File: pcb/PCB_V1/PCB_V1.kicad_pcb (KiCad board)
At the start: 4 copper layers, 100 x 100 mm, 170 parts, among them J201 UART / 3V3 logic, J301 SHT4x / XH 2.50, J302 FLOAT / 3.5 mm, J401 HRO TF-01A, J501 FAN1 / 3.5 mm, J511 FAN2 / 3.5 mm, J521 PUMP 24V / 6W, J601 PTC + / switched - (3.5 mm), J711 LED +/- (return isolated), J721 LED +/- (return isolated), J731 LED +/- (return isolated), J901 XT60PW-M 24V IN, Q501 AO3400A, Q511 AO3400A, Q521 AO3422, Q601 NTMFS5C628NLT1G, Q711 AOD66923, Q721 AOD66923, SW201 RESET, SW202 BOOT, U101 TPS54202DDCR, U201 ESP32-WROOM-32E-N4, U301 PCF8563T/5, U601 UCC27524ADR, U700 SN74LVC1G08DBVR, U710 AL8853S-13, U720 AL8853S-13, U902 LMR16020PDDAR, Y301 32.768k 12.5pF

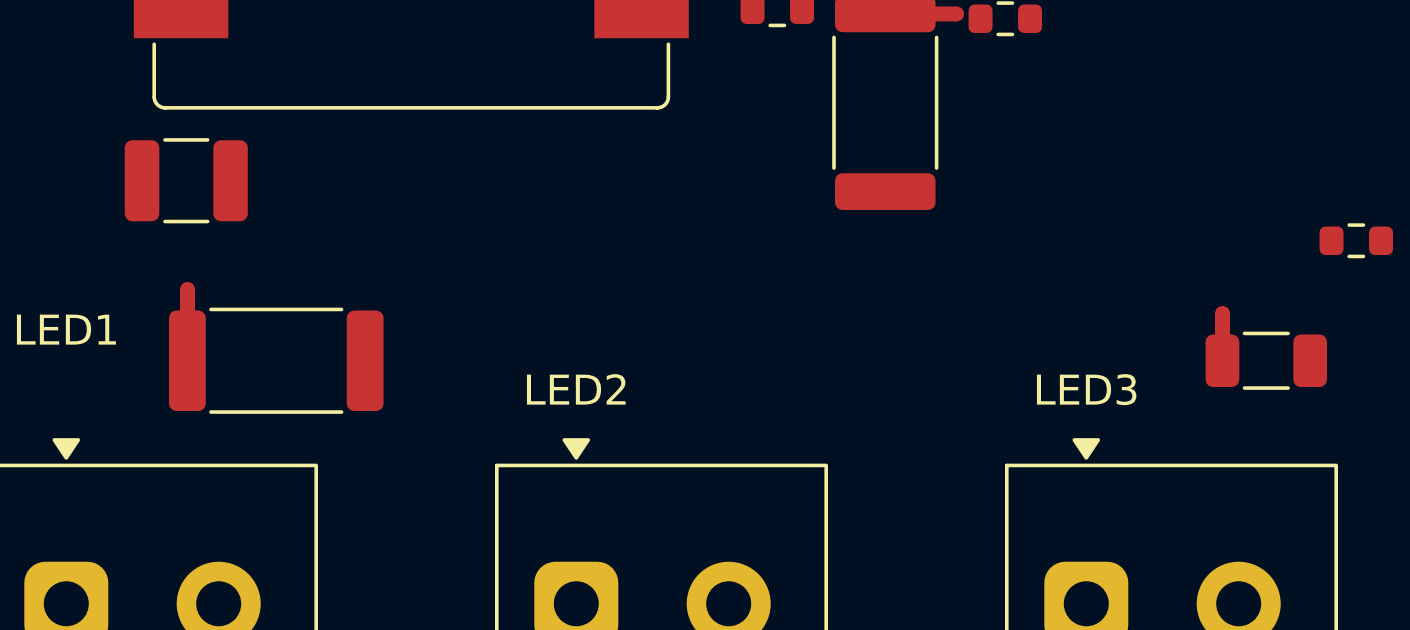
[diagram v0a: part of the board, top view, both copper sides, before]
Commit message: pcb: attach all 3D models to the board and check them
- sync_models.py --write attached the mechanical models (J901, J302,
  J501, J511, J521, J601, J711, J721, J731, F902, BT301, SW201, SW202);
  every placed part now has a 3D model.
- verify_placement.py fails when a placed part has no model or a
  ${KIPRJMOD} model file is missing.
- NT712/NT722 moved 0.1 mm away from R716/R726: 0.55 mm to the LED
  return pads, above the 0.5 mm LED48 clearance (the intermittent
  0.45 mm DRC report seen during PR #18).
- Checked in the KiCad 10 GUI 3D viewer (top, bottom with BT301,
  isometric) and the footprint editor 3D view; kicad-cli renders.
- F902 height stays calculated (17.15 mm); allow >= 18 mm until a
  sample is measured. SOURCES_mechanical.md and PLACEMENT.md updated.

Co-Authored-By: Claude Opus 5.5 <noreply@anthropic.com>
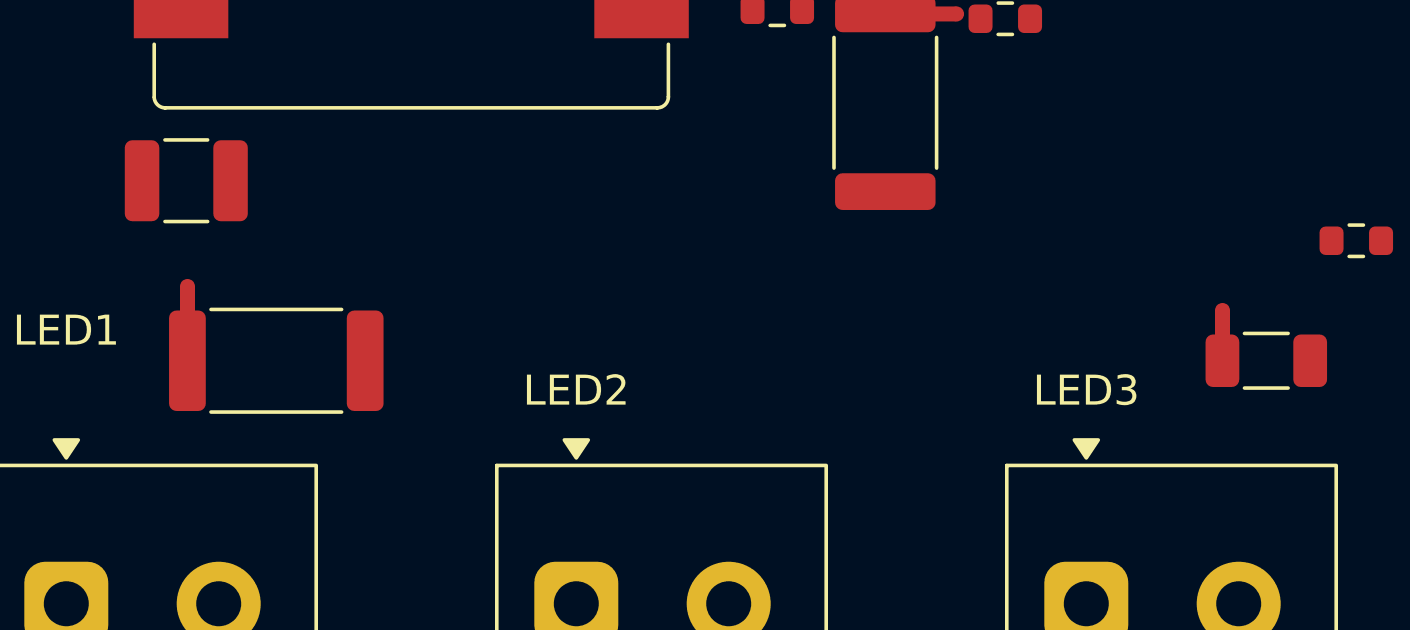
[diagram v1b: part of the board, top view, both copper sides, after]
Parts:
- moved NT722 0.10 mm to (98.5, 134.8)
- moved NT712 0.10 mm to (64.0, 134.0)
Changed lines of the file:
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@@
 		)
 		(embedded_fonts no)
+		(model "${KIPRJMOD}/libraries/GrowBox.3dshapes/TerminalBlock_DORABO_DB125-3.5_1x04_P3.50mm_Horizontal.step"
+			(offset
+				(xyz 0 0 0)
+			)
+			(scale
+				(xyz 1 1 1)
+			)
+			(rotate
+				(xyz 0 0 0)
+			)
+		)
 	)
 	(footprint "Capacitor_SMD:C_1210_3225Metric"
@@
 		)
 		(embedded_fonts no)
+		(model "${KIPRJMOD}/libraries/GrowBox.3dshapes/TerminalBlock_DORABO_DB125-3.5_1x04_P3.50mm_Horizontal.step"
+			(offset
+				(xyz 0 0 0)
+			)
+			(scale
+				(xyz 1 1 1)
+			)
+			(rotate
+				(xyz 0 0 0)
+			)
+		)
 	)
 	(footprint "Capacitor_SMD:C_0603_1608Metric"
@@
 		)
 		(embedded_fonts no)
+		(model "${KIPRJMOD}/libraries/GrowBox.3dshapes/TerminalBlock_DORABO_DB125-3.5_1x02_P3.50mm_Horizontal.step"
+			(offset
+				(xyz 0 0 0)
+			)
+			(scale
+				(xyz 1 1 1)
+			)
+			(rotate
+				(xyz 0 0 0)
+			)
+		)
 	)
 	(footprint "Button_Switch_SMD:SW_Push_1P1T_XKB_TS-1187A"
@@
 		)
 		(embedded_fonts no)
-		(model "${KICAD10_3DMODEL_DIR}/Button_Switch_SMD.3dshapes/SW_Push_1P1T_XKB_TS-1187A.step"
+		(model "${KIPRJMOD}/libraries/GrowBox.3dshapes/SW_Push_1P1T_XKB_TS-1187A.step"
 			(offset
 				(xyz 0 0 0)
@@
 		)
 		(embedded_fonts no)
+		(model "${KIPRJMOD}/libraries/GrowBox.3dshapes/TerminalBlock_DORABO_DB125-3.5_1x02_P3.50mm_Horizontal.step"
+			(offset
+				(xyz 0 0 0)
+			)
+			(scale
+				(xyz 1 1 1)
+			)
+			(rotate
+				(xyz 0 0 0)
+			)
+		)
 	)
 	(footprint "Capacitor_SMD:C_1210_3225Metric"
@@
 		)
 		(embedded_fonts no)
-		(model "${KICAD10_3DMODEL_DIR}/Connector_AMASS.3dshapes/AMASS_XT60PW-M_1x02_P7.20mm_Horizontal.step"
+		(model "${KIPRJMOD}/libraries/GrowBox.3dshapes/AMASS_XT60PW-M_1x02_P7.20mm_Horizontal.step"
 			(offset
 				(xyz 0 0 0)
@@
 		)
 		(embedded_fonts no)
+		(model "${KIPRJMOD}/libraries/GrowBox.3dshapes/TerminalBlock_KANGNEX_WJ500V-5.08_1x02_P5.08mm_Horizontal.step"
+			(offset
+				(xyz 0 0 0)
+			)
+			(scale
+				(xyz 1 1 1)
+			)
+			(rotate
+				(xyz 0 0 0)
+			)
+		)
 	)
 	(footprint "TestPoint:TestPoint_Pad_D2.0mm"
@@
 		)
 		(embedded_fonts no)
+		(model "${KIPRJMOD}/libraries/GrowBox.3dshapes/TerminalBlock_DORABO_DB125-3.5_1x02_P3.50mm_Horizontal.step"
+			(offset
+				(xyz 0 0 0)
+			)
+			(scale
+				(xyz 1 1 1)
+			)
+			(rotate
+				(xyz 0 0 0)
+			)
+		)
 	)
 	(footprint "Button_Switch_SMD:SW_Push_1P1T_XKB_TS-1187A"
@@
 		)
 		(embedded_fonts no)
-		(model "${KICAD10_3DMODEL_DIR}/Button_Switch_SMD.3dshapes/SW_Push_1P1T_XKB_TS-1187A.step"
+		(model "${KIPRJMOD}/libraries/GrowBox.3dshapes/SW_Push_1P1T_XKB_TS-1187A.step"
 			(offset
 				(xyz 0 0 0)
@@
 	(footprint "NetTie:NetTie-2_SMD_Pad0.5mm"
 		(layer "F.Cu")
-		(at 64.04 134.125 90)
+		(at 64.04 134.025 90)
 		(descr "Net tie, 2 pin, 0.5mm square SMD pads")
 		(tags "net tie")
@@
 		)
 		(embedded_fonts no)
+		(model "${KIPRJMOD}/libraries/GrowBox.3dshapes/TerminalBlock_KANGNEX_WJ500V-5.08_1x02_P5.08mm_Horizontal.step"
+			(offset
+				(xyz 0 0 0)
+			)
+			(scale
+				(xyz 1 1 1)
+			)
+			(rotate
+				(xyz 0 0 0)
+			)
+		)
 	)
 	(footprint "Capacitor_SMD:C_0603_1608Metric"
@@
 		)
 		(embedded_fonts no)
+		(model "${KIPRJMOD}/libraries/GrowBox.3dshapes/TerminalBlock_KANGNEX_WJ500V-5.08_1x02_P5.08mm_Horizontal.step"
+			(offset
+				(xyz 0 0 0)
+			)
+			(scale
+				(xyz 1 1 1)
+			)
+			(rotate
+				(xyz 0 0 0)
+			)
+		)
 	)
 	(footprint "Resistor_SMD:R_0603_1608Metric"
@@
 		)
 		(embedded_fonts no)
+		(model "${KIPRJMOD}/libraries/GrowBox.3dshapes/Fuseholder_Blade_Mini_XFCN_XF-508P.step"
+			(offset
+				(xyz 0 0 0)
+			)
+			(scale
+				(xyz 1 1 1)
+			)
+			(rotate
+				(xyz 0 0 0)
+			)
+		)
 	)
 	(footprint "NetTie:NetTie-2_SMD_Pad0.5mm"
 		(layer "F.Cu")
-		(at 98.54 134.925 90)
+		(at 98.54 134.825 90)
 		(descr "Net tie, 2 pin, 0.5mm square SMD pads")
 		(tags "net tie")
@@
 		)
 		(embedded_fonts no)
-		(model "${KICAD10_3DMODEL_DIR}/Battery.3dshapes/BatteryHolder_MYOUNG_BS-07-A1BJ001_CR2032.step"
+		(model "${KIPRJMOD}/libraries/GrowBox.3dshapes/BatteryHolder_MYOUNG_BS-07-A1BJ001_CR2032.step"
 			(offset
 				(xyz 0 0 0)

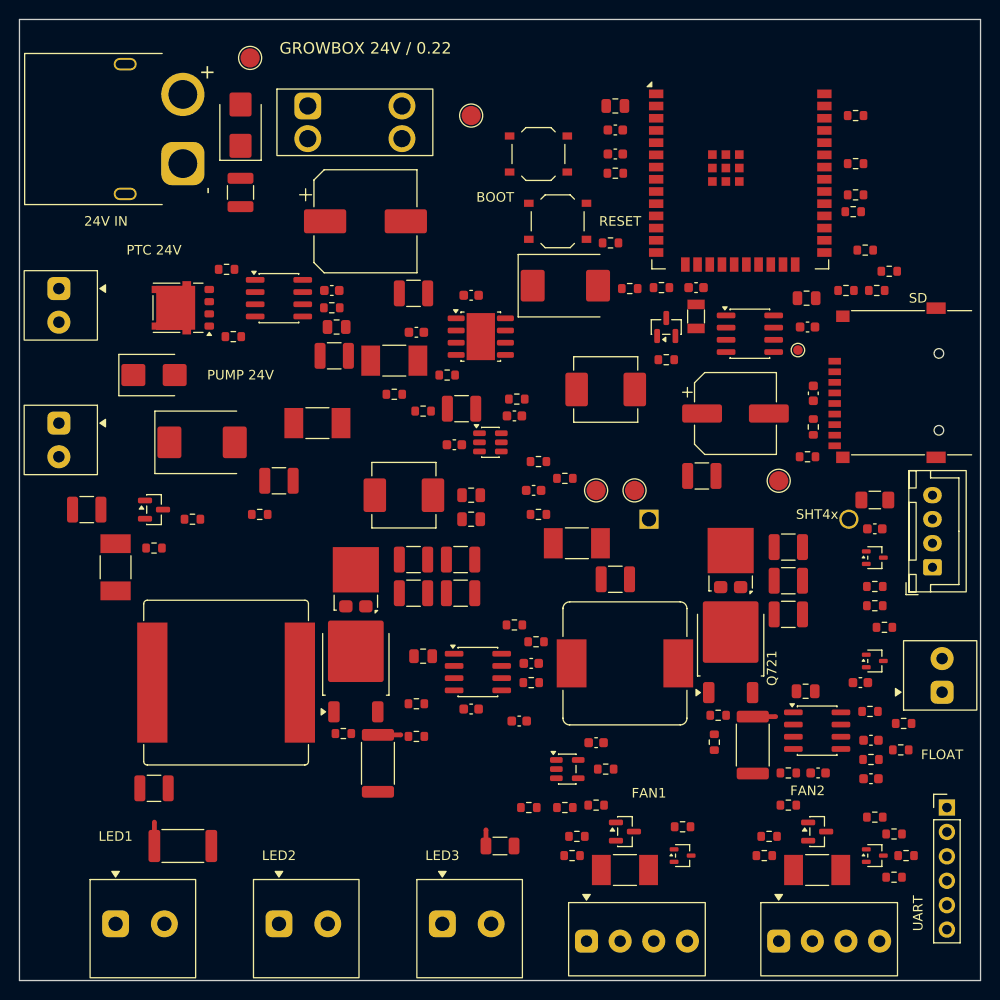
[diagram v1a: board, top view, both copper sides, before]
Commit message: pcb: route the board
First complete layout of 0.22: DRC 0 violations and 0 unconnected pads (also
after KiCad's own zone refill), In1 is a single GND plane without tracks,
909 tracks, 292 vias, GND pours on both outer layers, +3V3 fill on In2,
+24 V pours on F.Cu and B.Cu with 29 vias of 0.4 mm. check_all.py passes.

Co-Authored-By: Claude Sonnet 5.5 <noreply@anthropic.com>
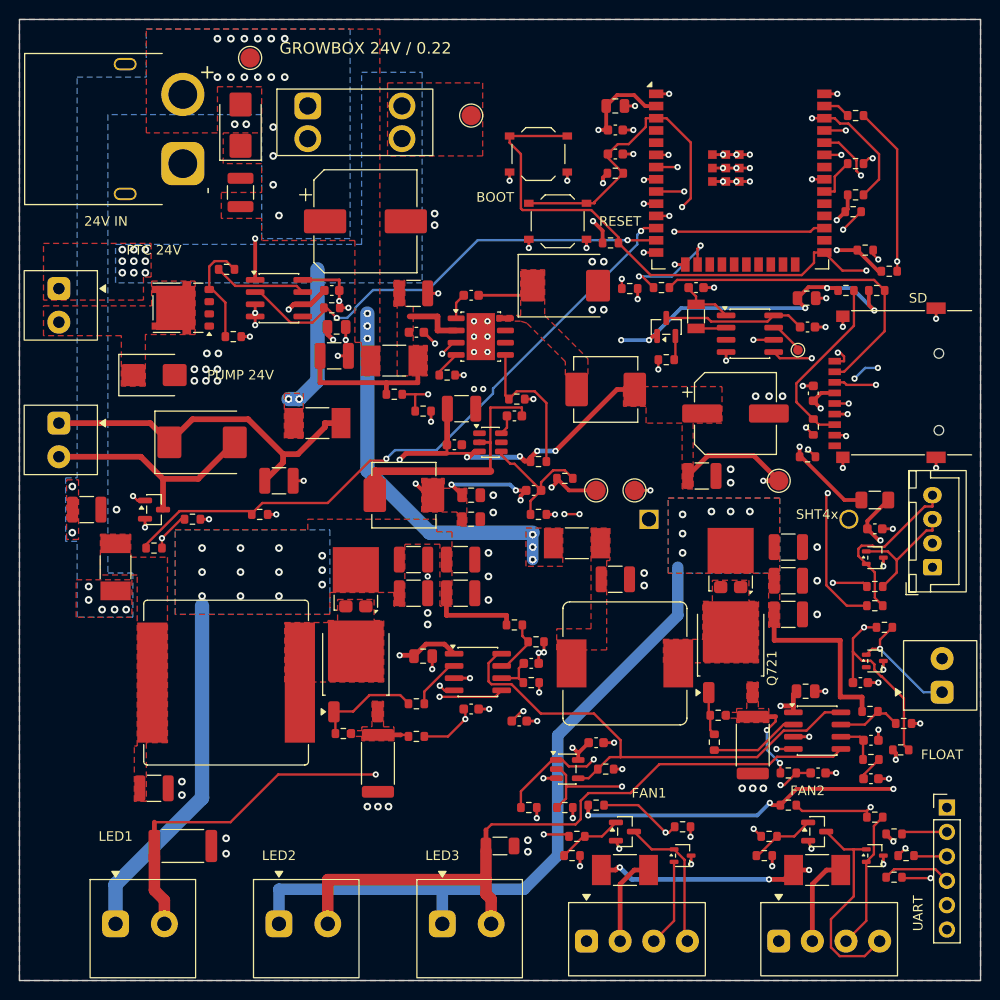
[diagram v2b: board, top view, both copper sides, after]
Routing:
- net +3V3: track 0.00 -> 283.6 mm, vias 0 -> 24
- net +12V: track 0.00 -> 172.1 mm, vias 0 -> 13
- net /MCU / ESP32/ESP_IO0: track 0.00 -> 129.3 mm, vias 0 -> 1
- net /MCU / ESP32/ESP_EN: track 0.00 -> 116.8 mm, vias 0 -> 1
- net LIGHT_ENABLE: track 0.00 -> 98.5 mm, vias 0 -> 2
- net /LEDDrivers/LED2_OUT: track 0.00 -> 91.1 mm, vias 0 -> 6
- net GND: track 0.00 -> 86.5 mm, vias 0 -> 130
- net FAN2_TACH: track 0.00 -> 86.0 mm, vias 0 -> 2
- net /MCU / ESP32/UART_RX0: track 0.00 -> 85.1 mm, vias 0 -> 2
- net /MCU / ESP32/UART_TX0: track 0.00 -> 82.4 mm, vias 0 -> 2
- net FAN1_TACH: track 0.00 -> 80.9 mm, vias 0 -> 2
- net WATER_LEVEL: track 0.00 -> 76.8 mm, vias 0 -> 2
- net LIGHT_PWM: track 0.00 -> 76.2 mm, vias 0 -> 2
- net FAN1_PWM: track 0.00 -> 75.4 mm, vias 0 -> 4
- net I2C_SCL: track 0.00 -> 75.0 mm, vias 0 -> 3
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- added copper zone on F.Cu, net +12V
- added copper zone on B.Cu, net +24V
- added copper zone on F.Cu, net +24V
- added copper zone on B.Cu, net +24V_LOADS
- added copper zone on F.Cu, net +24V_LOADS
- added copper zone on F.Cu, net +3V3
- added copper zone on In2.Cu, net +3V3
- added copper zone on F.Cu, net /InputPower/AUX_VIN
- added copper zone on F.Cu, net /InputPower/BUCK12_SW
- added copper zone on B.Cu, net /LEDDrivers/LED1_OUT
- added copper zone on F.Cu, net /LEDDrivers/LED1_OUT
- added copper zone on F.Cu, net /LEDDrivers/LED1_SOURCE
- added copper zone on F.Cu, net /LEDDrivers/LED1_SW
- added copper zone on F.Cu, net /LEDDrivers/LED1_VIN
- added copper zone on B.Cu, net /LEDDrivers/LED2_OUT
- added copper zone on F.Cu, net /LEDDrivers/LED2_OUT
- added copper zone on F.Cu, net /LEDDrivers/LED2_SOURCE
- added copper zone on F.Cu, net /LEDDrivers/LED2_SW
- added copper zone on F.Cu, net /LEDDrivers/LED2_VIN
- added copper zone on F.Cu, net /Outputs/Heater/HEATER_DRAIN
- added copper zone on B.Cu, net GND
- added copper zone on F.Cu, net GND
- added copper zone on In1.Cu, net GND
